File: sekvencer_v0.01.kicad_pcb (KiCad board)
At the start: 2 copper layers, 86.4 x 91.4 mm, 139 parts, among them J1 AVR_ISP_01X06, J10 50V_OUT, J11 BIAS_DIRECT, J12 50V_GND, J13 TERMISTOR, J14 50V_GND, J15 50V_GND, J16 50V_GND, J17 BIAS, J18 50V_GND, J19 50V_GND, J2 PTT, J3 SWR, J4 POWER, J5 LCD, J6 RX_REL, J7 TX_REL, J8 FAN, J9 50V_IN, Q1 BC857, Q2 BSS138, Q3 BSS138, Q4 IRLML0030TRPBF, Q5 BBS3002-TL-1E, Q6 BSS138, Q7 BC847, U1 ATmega328P-AU, U2 LP2950-5.0_TO252, U3 LM2576HVS-12, U4 LTC6101AHS5, U5 LP2951ACD-3.3R2G, Y1 LFXTAL071268CUTT 16MHz

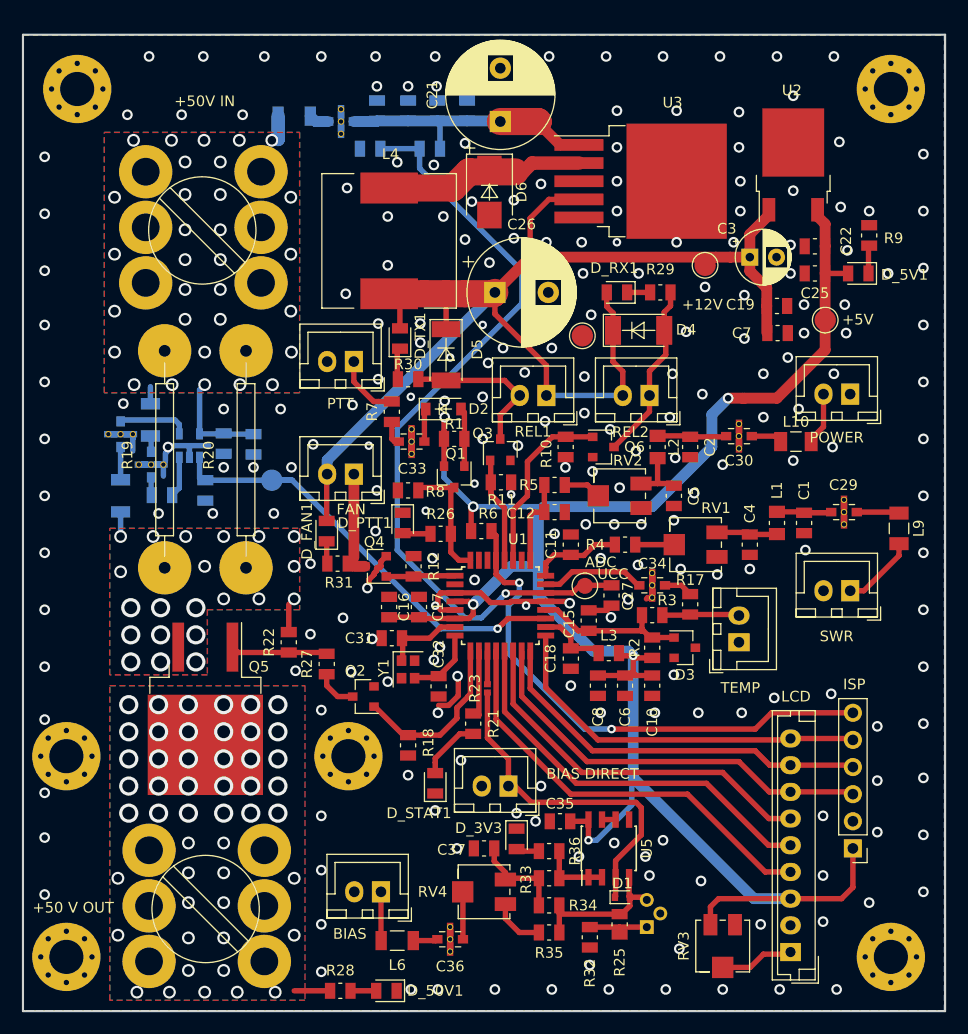
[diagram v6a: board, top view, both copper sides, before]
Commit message: add partial schematics images, complete schematic good version for publi
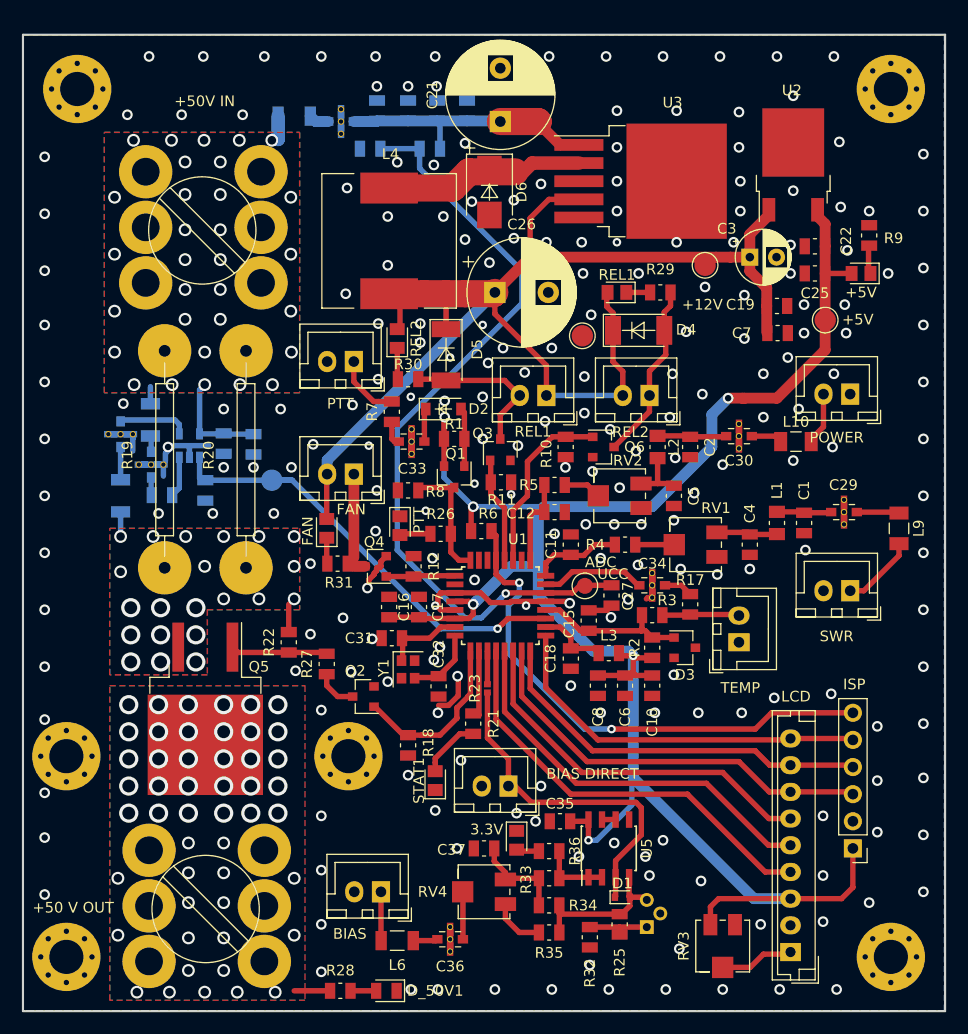
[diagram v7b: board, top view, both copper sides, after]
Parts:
- removed D_3V3, D_5V1, D_FAN1, D_PTT1, D_RX1, D_STAT1, D_TX1: LH R974-LP-1, LED_SMD:LED_0805_2012Metric
- added D10: FAN, LED_SMD:LED_0805_2012Metric, F.Cu at (175.8, 94.5)
- added D11: +5V, LED_SMD:LED_0805_2012Metric, F.Cu at (225.8, 70.6)
- added D12: PTT, LED_SMD:LED_0805_2012Metric, F.Cu at (182.6, 94.2)
- added D13: 3.3V, LED_SMD:LED_0805_2012Metric, F.Cu at (193.5, 123.7)
- added D7: STAT1, LED_SMD:LED_0805_2012Metric, F.Cu at (185.9, 118.1)
- added D8: REL1, LED_SMD:LED_0805_2012Metric, F.Cu at (202.9, 72.4)
- added D9: REL2, LED_SMD:LED_0805_2012Metric, F.Cu at (182.4, 76.7)
- J4: value POWER -> PWR
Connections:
- net /ADC_POWER renamed /ADC_PWR
- net Net-(C31-Pad1) renamed /XTAL1
- net Net-(C32-Pad1) renamed /XTAL2
- J14 pad 1: Net-(J14-Pad1) -> GND
- J15 pad 1: Net-(J15-Pad1) -> GND
- J16 pad 1: Net-(J16-Pad1) -> GND
- J19 pad 1: Net-(J19-Pad1) -> GND
